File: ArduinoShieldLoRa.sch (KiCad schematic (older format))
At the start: 17 parts, among them J1 CONN_01X03, P1 Power, P2 Analog, P3 Digital, P4 Digital, P5 CONN_01X01, P6 CONN_01X01, P7 CONN_01X01, P8 CONN_01X01, U1 RFM95, U2 74HC4050D, U3 AP2112K-3.3

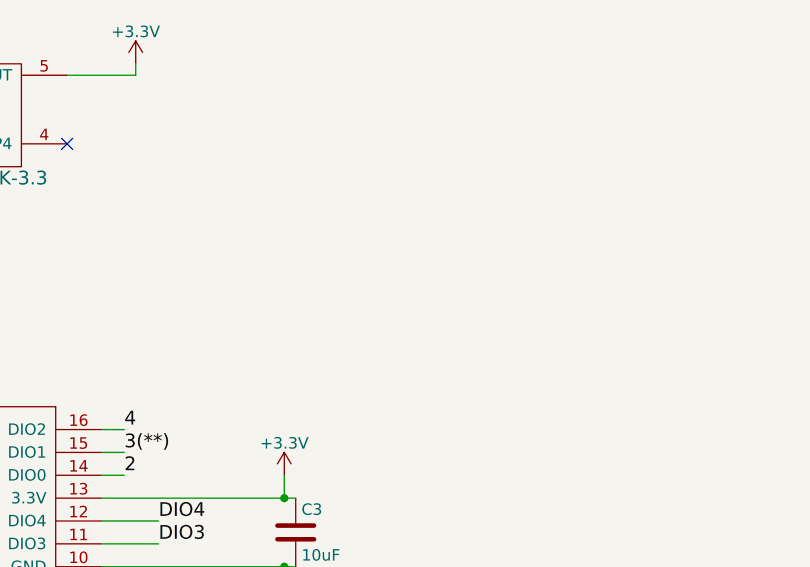
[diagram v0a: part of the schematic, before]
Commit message: Add resistors
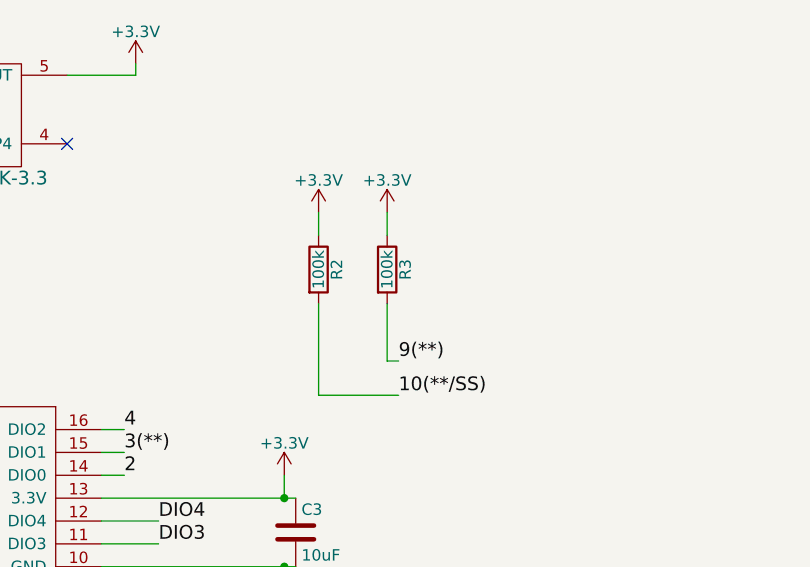
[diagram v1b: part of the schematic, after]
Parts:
- added R2, R3: 100k, symbol R
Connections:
- net +3V3: now also R2.1, R3.1
- net 10(**/SS): now also R2.2
- net 9(**): now also R3.2
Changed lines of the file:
@@
 NoConn ~ 10550 1200
 NoConn ~ 10550 1300
+$Comp
+L R R2
+U 1 1 59409DD6
+P 6350 3350
+F 0 "R2" V 6430 3350 50  0000 C CNN
+F 1 "100k" V 6350 3350 50  0000 C CNN
+F 2 "" V 6280 3350 50  0001 C CNN
+F 3 "" H 6350 3350 50  0001 C CNN
+	1    6350 3350
+	1    0    0    -1
+$EndComp
+$Comp
+L R R3
+U 1 1 59409EAC
+P 6650 3350
+F 0 "R3" V 6730 3350 50  0000 C CNN
+F 1 "100k" V 6650 3350 50  0000 C CNN
+F 2 "" V 6580 3350 50  0001 C CNN
+F 3 "" H 6650 3350 50  0001 C CNN
+	1    6650 3350
+	1    0    0    -1
+$EndComp
+$Comp
+L +3.3V #PWR?
+U 1 1 59409EFD
+P 6350 3100
+F 0 "#PWR?" H 6350 2950 50  0001 C CNN
+F 1 "+3.3V" H 6350 3240 50  0000 C CNN
+F 2 "" H 6350 3100 50  0001 C CNN
+F 3 "" H 6350 3100 50  0001 C CNN
+	1    6350 3100
+	1    0    0    -1
+$EndComp
+$Comp
+L +3.3V #PWR?
+U 1 1 59409FB3
+P 6650 3100
+F 0 "#PWR?" H 6650 2950 50  0001 C CNN
+F 1 "+3.3V" H 6650 3240 50  0000 C CNN
+F 2 "" H 6650 3100 50  0001 C CNN
+F 3 "" H 6650 3100 50  0001 C CNN
+	1    6650 3100
+	1    0    0    -1
+$EndComp
+Wire Wire Line
+	6350 3100 6350 3200
+Wire Wire Line
+	6650 3100 6650 3200
+Text Label 6700 3900 0    60   ~ 0
+10(**/SS)
+Text Label 6700 3750 0    60   ~ 0
+9(**)
+Wire Wire Line
+	6700 3750 6650 3750
+Wire Wire Line
+	6650 3750 6650 3500
+Wire Wire Line
+	6700 3900 6350 3900
+Wire Wire Line
+	6350 3900 6350 3500
 $EndSCHEMATC

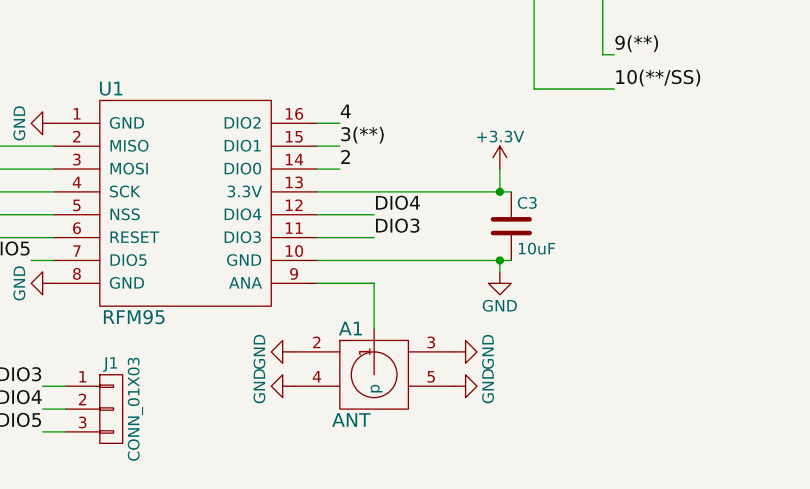
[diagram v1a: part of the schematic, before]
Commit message: add pin for cable as antenna
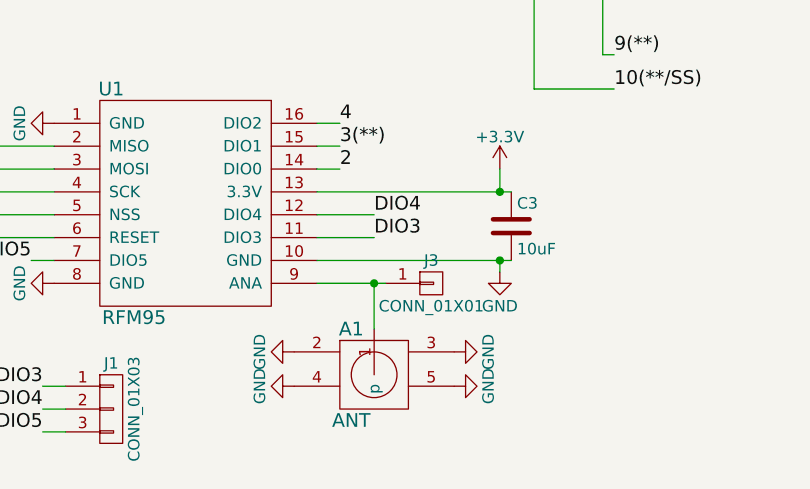
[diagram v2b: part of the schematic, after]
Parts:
- added J3: CONN_01X01, Wire_Pads:SolderWirePad_single_0-8mmDrill, symbol CONN_01X01
- R2, R3: footprint (none) -> Resistors_SMD:R_0603_HandSoldering; #manf (none) -> RCA0603100KJNEC
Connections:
- net at A1.1 (p), U1.9 (ANA): now also J3.1 (P1)
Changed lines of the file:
@@
 EESchema Schematic File Version 2
+LIBS:ArduinoShieldLoRa-rescue
 LIBS:power
 LIBS:device
@@
 	6250 4650 5400 4650
 Wire Wire Line
-	5400 4750 5650 4750
+	5400 4750 5700 4750
 Wire Wire Line
 	5650 4750 5650 4950
@@
 F 0 "R2" V 6430 3350 50  0000 C CNN
 F 1 "100k" V 6350 3350 50  0000 C CNN
-F 2 "" V 6280 3350 50  0001 C CNN
+F 2 "Resistors_SMD:R_0603_HandSoldering" V 6280 3350 50  0001 C CNN
 F 3 "" H 6350 3350 50  0001 C CNN
+F 4 "RCA0603100KJNEC" V 6350 3350 60  0001 C CNN "#manf"
 	1    6350 3350
 	1    0    0    -1
@@
 F 0 "R3" V 6730 3350 50  0000 C CNN
 F 1 "100k" V 6650 3350 50  0000 C CNN
-F 2 "" V 6580 3350 50  0001 C CNN
+F 2 "Resistors_SMD:R_0603_HandSoldering" V 6580 3350 50  0001 C CNN
 F 3 "" H 6650 3350 50  0001 C CNN
+F 4 "RCA0603100KJNEC" V 6650 3350 60  0001 C CNN "#manf"
 	1    6650 3350
 	1    0    0    -1
 $EndComp
 $Comp
-L +3.3V #PWR?
+L +3.3V #PWR017
 U 1 1 59409EFD
 P 6350 3100
-F 0 "#PWR?" H 6350 2950 50  0001 C CNN
+F 0 "#PWR017" H 6350 2950 50  0001 C CNN
 F 1 "+3.3V" H 6350 3240 50  0000 C CNN
 F 2 "" H 6350 3100 50  0001 C CNN
@@
 $EndComp
 $Comp
-L +3.3V #PWR?
+L +3.3V #PWR018
 U 1 1 59409FB3
 P 6650 3100
-F 0 "#PWR?" H 6650 2950 50  0001 C CNN
+F 0 "#PWR018" H 6650 2950 50  0001 C CNN
 F 1 "+3.3V" H 6650 3240 50  0000 C CNN
 F 2 "" H 6650 3100 50  0001 C CNN
@@
 Wire Wire Line
 	6350 3900 6350 3500
+$Comp
+L CONN_01X01 J3
+U 1 1 5941DDAF
+P 5900 4750
+F 0 "J3" H 5900 4850 50  0000 C CNN
+F 1 "CONN_01X01" H 5900 4650 50  0000 C CNN
+F 2 "Wire_Pads:SolderWirePad_single_0-8mmDrill" H 5900 4750 50  0001 C CNN
+F 3 "" H 5900 4750 50  0001 C CNN
+	1    5900 4750
+	1    0    0    -1
+$EndComp
+Connection ~ 5650 4750
 $EndSCHEMATC

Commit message: add gitignore
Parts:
- A1: symbol ANT -> ANT-RESCUE-ArduinoShieldLoRa
- U1: symbol RFM95 -> RFM95-RESCUE-ArduinoShieldLoRa
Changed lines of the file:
@@
 $EndComp
 $Comp
-L RFM95 U1
+L RFM95-RESCUE-ArduinoShieldLoRa U1
 U 1 1 593EC92C
 P 4600 4900
@@
 $EndComp
 $Comp
-L ANT A1
+L ANT-RESCUE-ArduinoShieldLoRa A1
 U 1 1 593ECA41
 P 5300 5350

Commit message: update library
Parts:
- removed U1: RFM95, ArduinoShieldLoRa:RFM95, symbol RFM95-RESCUE-ArduinoShieldLoRa
- added U?: RFM95, symbol RFM95-RESCUE-ArduinoShieldLoRa
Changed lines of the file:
@@
 LIBS:valves
 LIBS:74HC4050D
-LIBS:rfm95
-LIBS:NodeLoRaGroveKitty-cache
+LIBS:ArduinoShieldLoRa
 LIBS:ArduinoShieldLoRa-cache
 EELAYER 25 0
@@
 $EndComp
 $Comp
-L RFM95-RESCUE-ArduinoShieldLoRa U1
-U 1 1 593EC92C
-P 4600 4900
-F 0 "U1" H 4500 5900 60  0000 C CNN
-F 1 "RFM95" H 4600 4900 60  0000 C CNN
-F 2 "ArduinoShieldLoRa:RFM95" H 4600 4900 60  0001 C CNN
-F 3 "" H 4600 4900 60  0000 C CNN
-	1    4600 4900
-	1    0    0    -1
-$EndComp
-$Comp
 L ANT-RESCUE-ArduinoShieldLoRa A1
 U 1 1 593ECA41
@@
 $EndComp
 Connection ~ 5650 4750
+$Comp
+L RFM95-RESCUE-ArduinoShieldLoRa U?
+U 1 1 5B05A30B
+P 4600 4900
+F 0 "U?" H 4500 5900 60  0000 C CNN
+F 1 "RFM95" H 4600 4900 60  0000 C CNN
+F 2 "" H 4600 4900 60  0000 C CNN
+F 3 "" H 4600 4900 60  0000 C CNN
+	1    4600 4900
+	1    0    0    -1
+$EndComp
 $EndSCHEMATC
